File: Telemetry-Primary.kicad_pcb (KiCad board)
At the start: 2 copper layers, 94.5 x 82 mm, 152 parts, among them J1 CAN_LogicAnalyzer, J10 SMAConn, J11 USB_B_Micro, J12 CAN_In, J13 CAN_Out, J2 IMU_LogicAnalyzer, J3 GPS_LogicAnalyzer, J4 RTCC_LogicAnalyzer, J5 SDCard_LogicAnalyzer, J6 SWD, J7 PowerConn, J8 RJ45_Abracon_ARJP11A-MASA-B-A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, J9 Micro_SD_Card_Det, SW1 Reset, SW2 RTCC_BattCheck, SW3 GPS_BattCheck, U1 STM32F429ZITx, U10 ADM3055E, U11 CDSOT23-T24CAN, U2 RI3-1205S, U3 NCP1117-3.3_SOT223, U4 LAN8742A-CZ-TR, U5 USBLC6-4SC6, U6 PCF8523T, U7 MTK3339, U8 BNO055, U9 CP2102N-A01-GQFN24, Y1 8M, Y2 25M, Y3 32.768k

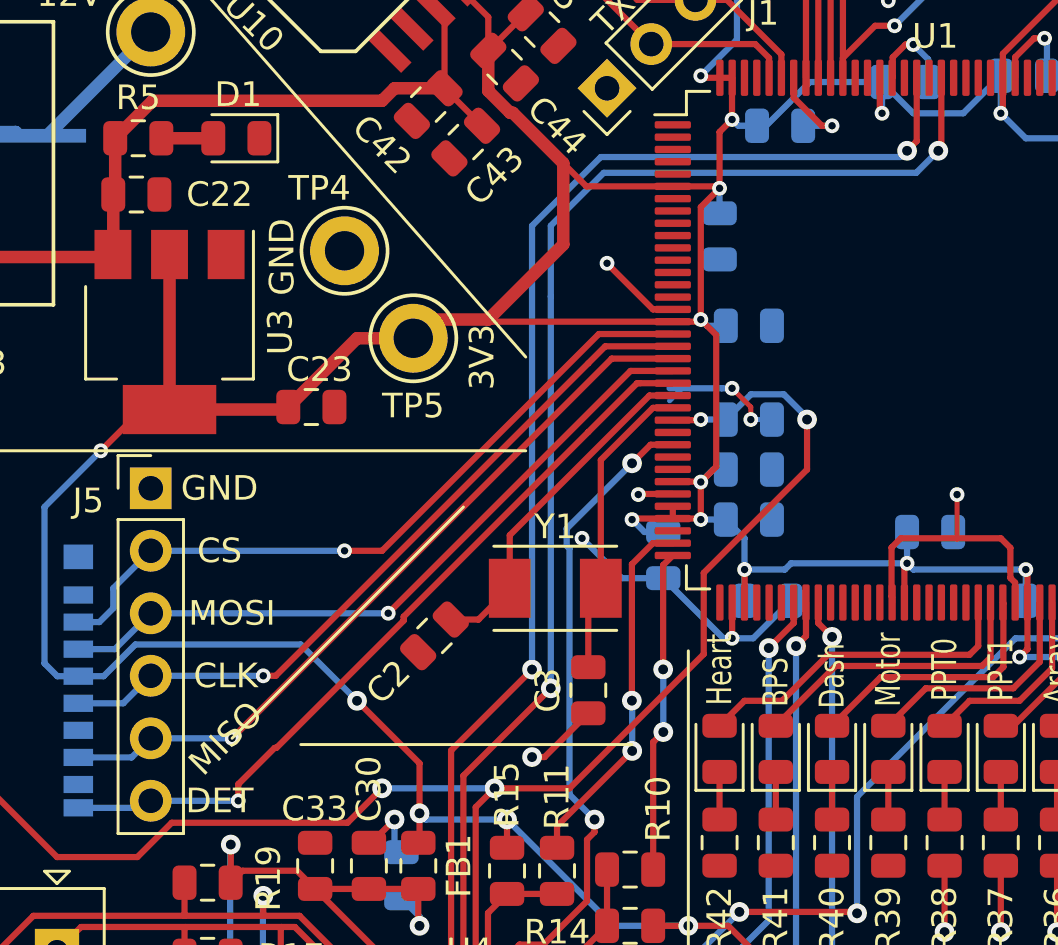
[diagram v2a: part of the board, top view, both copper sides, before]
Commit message: Fix routing near crystal.
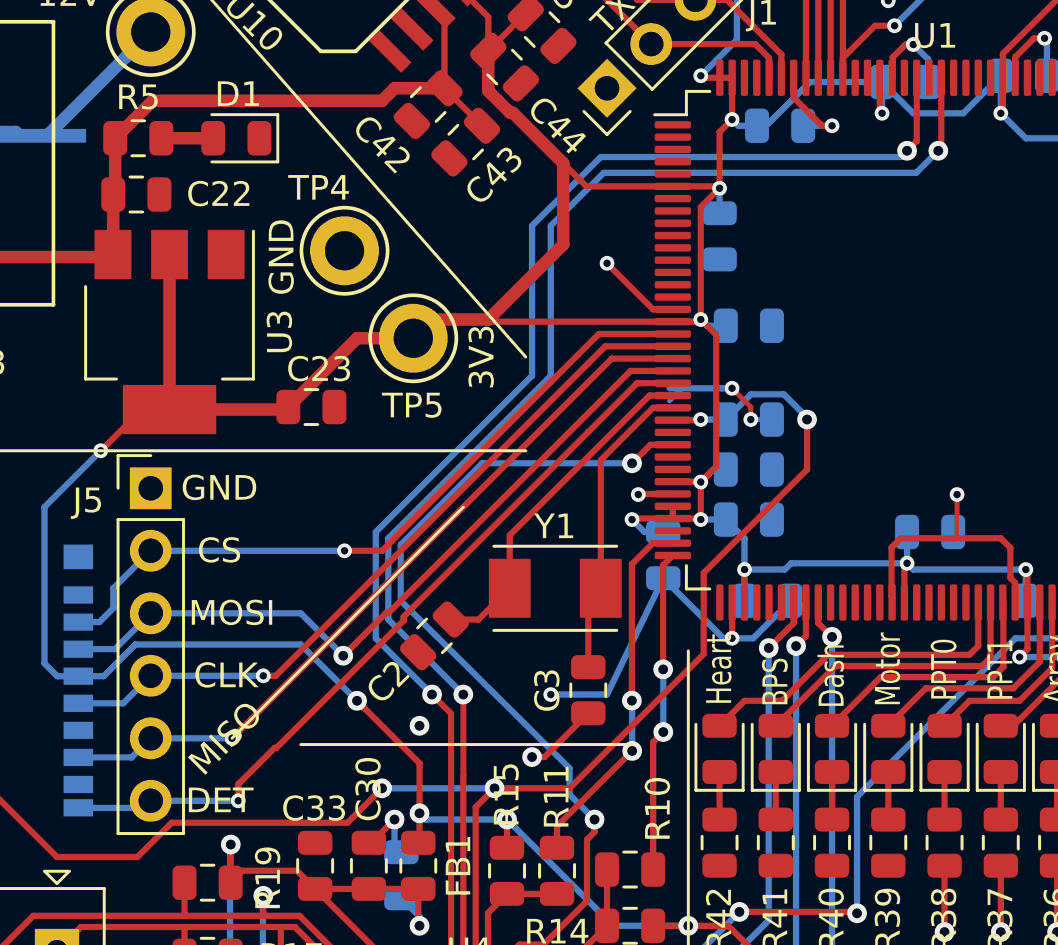
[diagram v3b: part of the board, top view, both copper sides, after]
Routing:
- net /RMII_MDC: track 27.1 -> 36.3 mm
- net GND: track 142.6 -> 146.2 mm, vias 33 -> 34
- net /RMII_TXD0: track 52.0 -> 54.6 mm
- net /RMII_TX_EN: track 52.6 -> 55.1 mm
- net /SPI5_MOSI: track 28.8 -> 30.3 mm

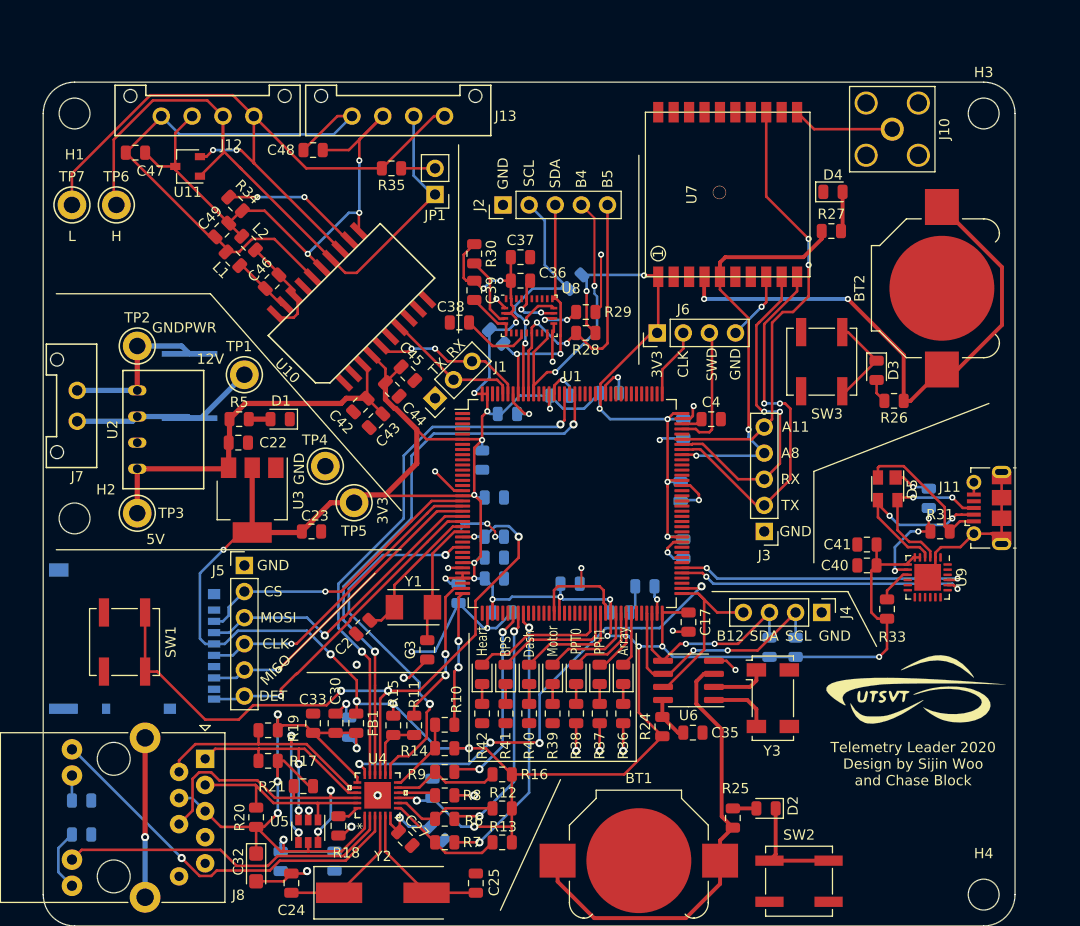
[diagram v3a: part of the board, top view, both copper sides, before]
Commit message: Makes mounting hole text invisible and updates title
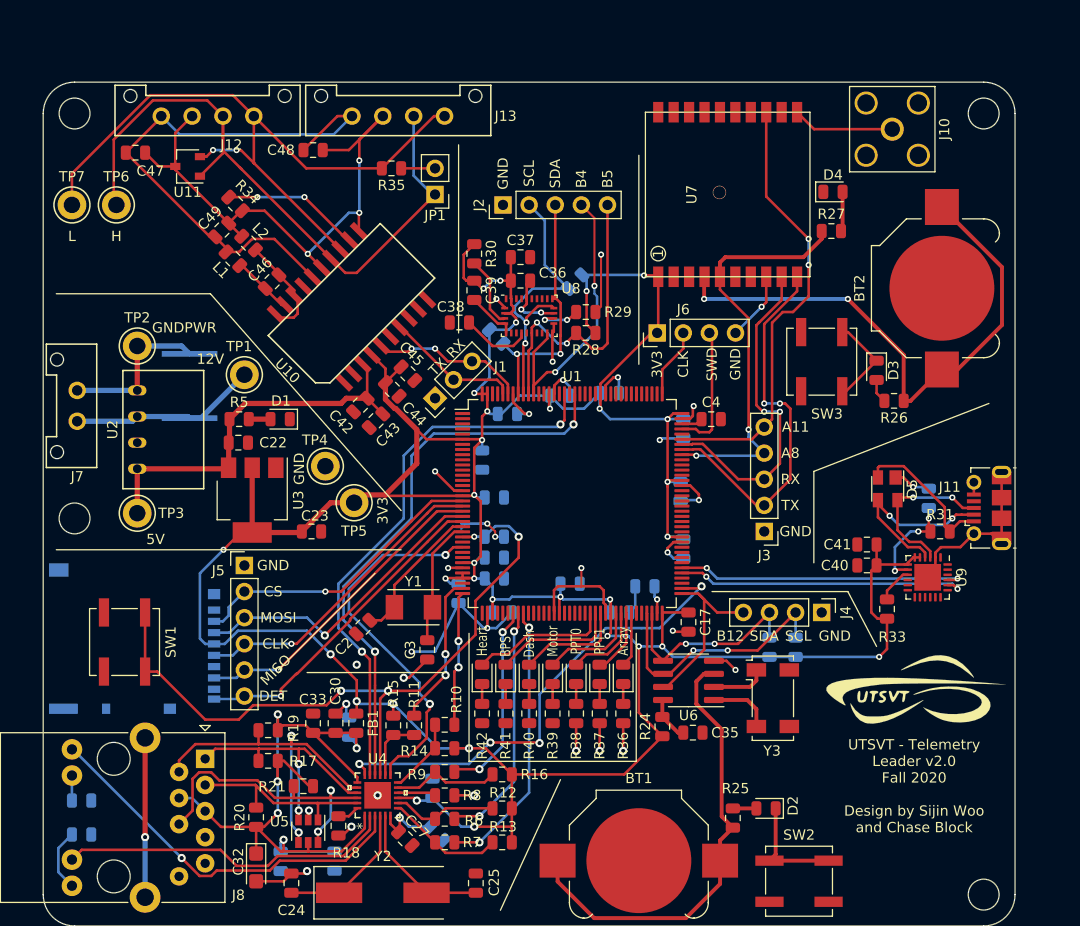
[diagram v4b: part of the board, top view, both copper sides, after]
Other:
- board text added: "UTSVT - Telemetry Leader v2.0 Fall 2020 Design by Sijin Woo and Chase Block"
- board text removed: "Telemetry Leader 2020 Design by Sijin Woo and Chase Block"
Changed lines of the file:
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@@
-(kicad_pcb (version 20171130) (host pcbnew 5.1.7-a382d34a8~87~ubuntu20.04.1)
+(kicad_pcb (version 20171130) (host pcbnew "(5.1.5)-3")
   (general
     (thickness 1.6)
@@
   )
   (setup
-    (last_trace_width 0.254)
+    (last_trace_width 0.25)
     (user_trace_width 0.2032)
     (user_trace_width 0.254)
@@
     (tags "mounting hole 3mm no annular")
     (attr virtual)
-    (fp_text reference H4 (at 0 -4) (layer F.SilkS)
+    (fp_text reference H4 (at 0 -4) (layer F.SilkS) hide
       (effects (font (size 1 1) (thickness 0.15)))
     )
@@
     (tags "mounting hole 3mm no annular")
     (attr virtual)
-    (fp_text reference H3 (at 0 -4) (layer F.SilkS)
+    (fp_text reference H3 (at 0 -4) (layer F.SilkS) hide
       (effects (font (size 1 1) (thickness 0.15)))
     )
@@
     (tags "mounting hole 3mm no annular")
     (attr virtual)
-    (fp_text reference H2 (at -4.130918 -0.179605 180) (layer F.SilkS)
+    (fp_text reference H2 (at -4.130918 -0.179605 180) (layer F.SilkS) hide
       (effects (font (size 1 1) (thickness 0.15)))
     )
@@
     (tags "mounting hole 3mm no annular")
     (attr virtual)
-    (fp_text reference H1 (at 0 -4) (layer F.SilkS)
+    (fp_text reference H1 (at 0 -4) (layer F.SilkS) hide
       (effects (font (size 1 1) (thickness 0.15)))
     )
@@
   (gr_line (start 129.032 72.39) (end 129.032 52.07) (layer F.SilkS) (width 0.12))
   (gr_line (start 111.506 69.342) (end 111.506 51.054) (layer F.SilkS) (width 0.12))
-  (gr_text "Telemetry Leader 2020\nDesign by Sijin Woo\nand Chase Block" (at 155.702 111.252) (layer F.SilkS)
+  (gr_text "UTSVT - Telemetry \nLeader v2.0\nFall 2020\n\nDesign by Sijin Woo\nand Chase Block" (at 155.8 113.4) (layer F.SilkS)
     (effects (font (size 1 1) (thickness 0.15)))
   )

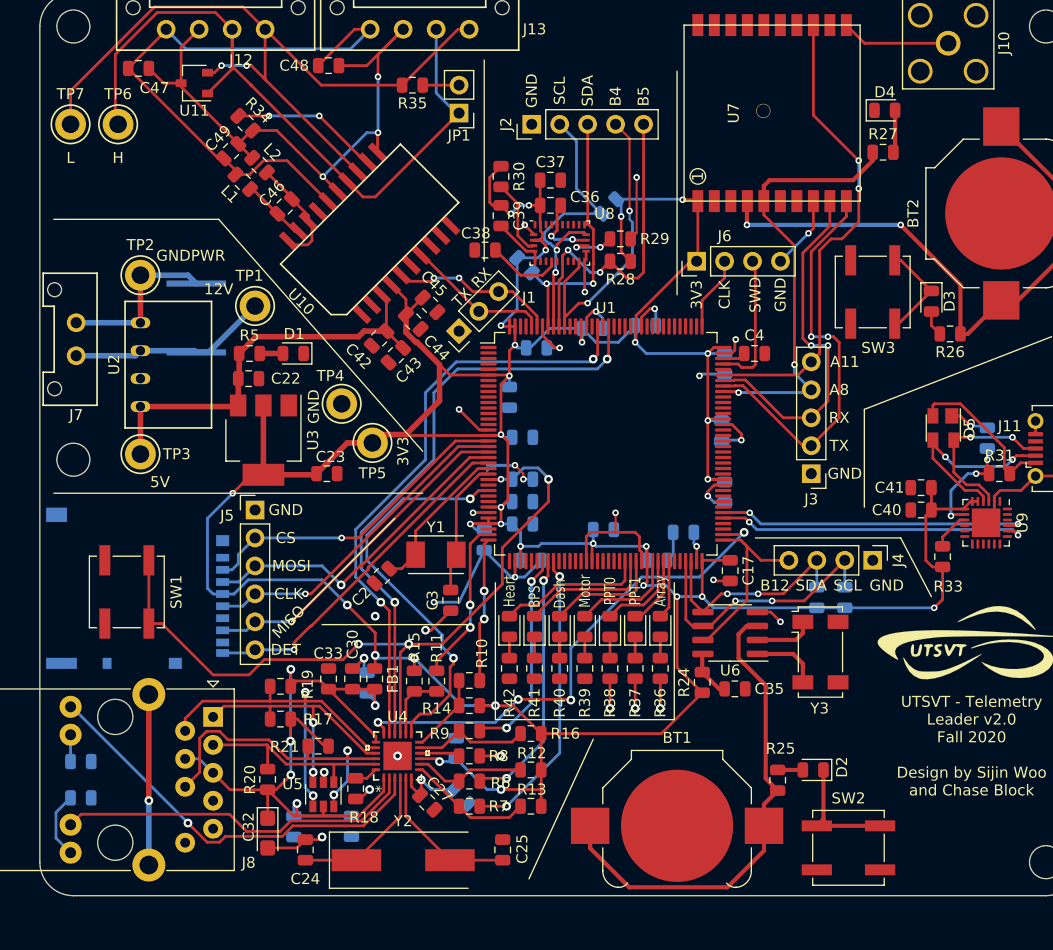
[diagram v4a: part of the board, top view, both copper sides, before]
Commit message: Some changes to solve errata and list of errata in v1
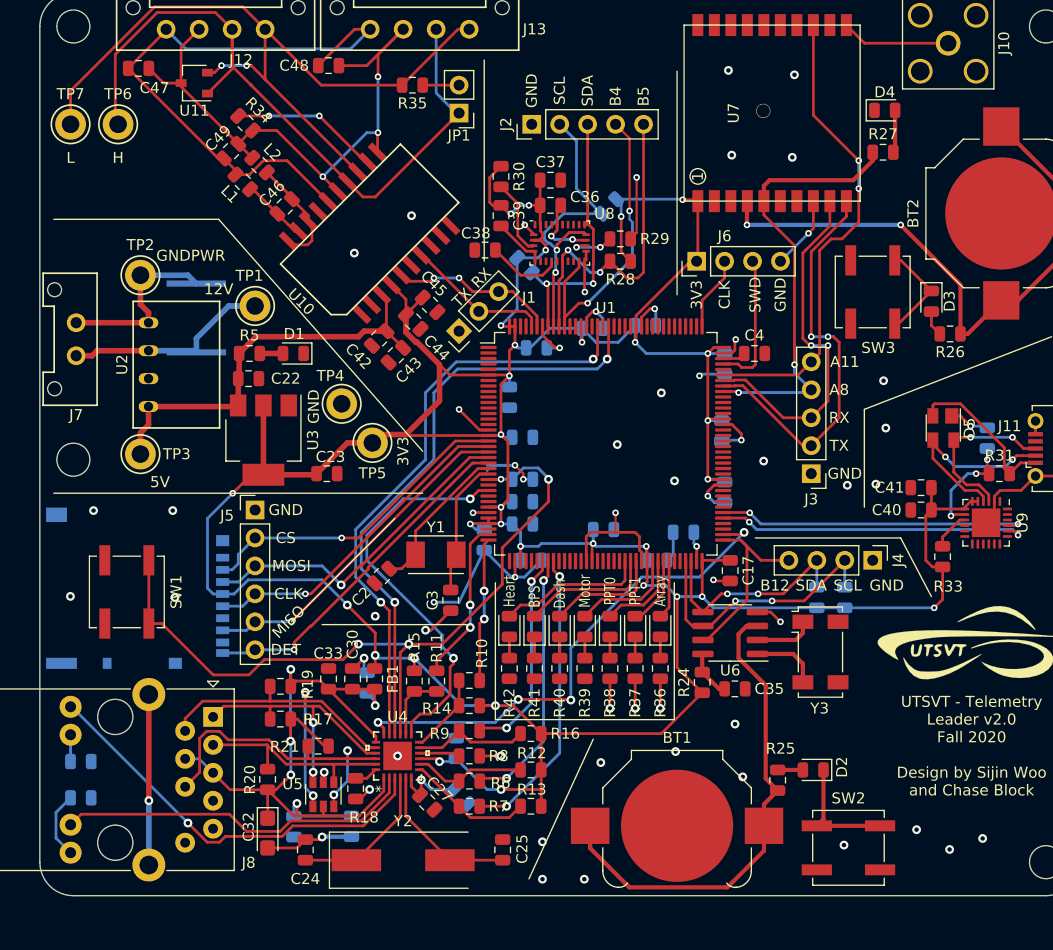
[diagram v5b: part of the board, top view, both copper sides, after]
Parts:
- moved U2 0.74 mm to (81.0, 78.7)
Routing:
- net GND: track 146.2 -> 148.9 mm, vias 34 -> 63
- net GNDPWR: track 15.6 -> 16.6 mm
- net +12V: track 18.3 -> 19.0 mm
